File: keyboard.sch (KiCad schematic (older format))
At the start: 149 parts

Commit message: Minor Changes On Schematic
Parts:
- gave numbers to parts that had none: 2
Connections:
- wire segments 325 -> 261
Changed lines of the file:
@@
 $EndComp
 $Comp
-L D D?
+L D D05
 U 1 1 57519F72
 P 3150 8400
-F 0 "D?" H 3150 8500 50  0000 C CNN
+F 0 "D05" H 3150 8500 50  0000 C CNN
 F 1 "D" H 3150 8300 50  0000 C CNN
 F 2 "" H 3150 8400 50  0000 C CNN
@@
 $EndComp
 $Comp
-L D D?
+L D D10
 U 1 1 57519F81
 P 3900 8600
-F 0 "D?" H 3900 8700 50  0000 C CNN
+F 0 "D10" H 3900 8700 50  0000 C CNN
 F 1 "D" H 3900 8500 50  0000 C CNN
 F 2 "" H 3900 8600 50  0000 C CNN
@@
 	11850 2650 12050 2650
 Wire Wire Line
-	13200 2400 13200 2600
-Wire Wire Line
-	13200 2600 13200 2800
+	13200 2400 13200 2800
 Wire Wire Line
 	12600 2800 12800 2800
@@
 	11850 4050 12050 4050
 Wire Wire Line
-	3450 5150 3450 5350
-Wire Wire Line
-	3450 5350 3450 5600
+	3450 5150 3450 5600
 Wire Wire Line
 	4200 5150 4200 5400
@@
 	11100 5400 11300 5400
 Wire Wire Line
-	12450 5150 12450 5350
-Wire Wire Line
-	12450 5350 12450 5400
-Wire Wire Line
-	3450 6500 3450 6750
-Wire Wire Line
-	3450 6750 3450 7000
+	12450 5150 12450 5400
+Wire Wire Line
+	3450 6500 3450 7000
 Wire Wire Line
 	4200 6500 4200 6750
@@
 	11100 6750 11300 6750
 Wire Wire Line
-	12450 6500 12450 6700
-Wire Wire Line
-	12450 6700 12450 7000
+	12450 6500 12450 7000
 Wire Wire Line
 	12450 7000 12350 7000
@@
 	11850 7000 12050 7000
 Wire Wire Line
-	3450 7900 3450 8150
-Wire Wire Line
-	3450 8150 3450 8400
-Wire Wire Line
-	4200 7900 4200 8150
-Wire Wire Line
-	4200 8150 4200 8200
-Wire Wire Line
-	4950 7900 4950 8150
-Wire Wire Line
-	4950 8150 4950 8400
-Wire Wire Line
-	7200 7900 7200 8150
-Wire Wire Line
-	7200 8150 7200 8350
-Wire Wire Line
-	7200 8350 7200 8550
+	3450 7900 3450 8400
+Wire Wire Line
+	4200 7900 4200 8200
+Wire Wire Line
+	4950 7900 4950 8400
+Wire Wire Line
+	7200 7900 7200 8550
 Wire Wire Line
 	10200 7900 10200 8150
@@
 	9600 8150 9800 8150
 Wire Wire Line
-	10950 7900 10950 8150
-Wire Wire Line
-	10950 8150 10950 8400
-Wire Wire Line
-	11700 7900 11700 8150
-Wire Wire Line
-	11700 8150 11700 8400
-Wire Wire Line
-	11700 8400 11700 8650
-Wire Wire Line
-	12450 7900 12450 8150
-Wire Wire Line
-	12450 8150 12450 8500
-Wire Wire Line
-	13200 7900 13200 8100
-Wire Wire Line
-	13200 8100 13200 8450
-Wire Wire Line
-	1650 2150 3050 2150
-Wire Wire Line
-	3050 2150 3800 2150
-Wire Wire Line
-	3800 2150 12700 2150
-Wire Wire Line
-	12700 2150 13850 2150
-Wire Wire Line
-	1650 3550 3050 3550
-Wire Wire Line
-	3050 3550 13850 3550
-Wire Wire Line
-	1650 4900 2950 4900
-Wire Wire Line
-	2950 4900 3050 4900
-Wire Wire Line
-	3050 4900 11950 4900
-Wire Wire Line
-	11950 4900 12650 4900
-Wire Wire Line
-	12650 4900 12700 4900
-Wire Wire Line
-	12700 4900 13200 4900
-Wire Wire Line
-	13200 4900 13850 4900
-Wire Wire Line
-	1650 6250 2950 6250
-Wire Wire Line
-	2950 6250 3050 6250
-Wire Wire Line
-	3050 6250 11950 6250
-Wire Wire Line
-	11950 6250 13850 6250
-Wire Wire Line
-	1650 7650 2900 7650
-Wire Wire Line
-	2900 7650 2950 7650
-Wire Wire Line
-	2950 7650 3050 7650
-Wire Wire Line
-	3050 7650 3650 7650
-Wire Wire Line
-	3650 7650 3700 7650
-Wire Wire Line
-	3700 7650 3800 7650
-Wire Wire Line
-	3800 7650 4450 7650
-Wire Wire Line
-	4450 7650 6650 7650
-Wire Wire Line
-	6650 7650 6700 7650
-Wire Wire Line
-	6700 7650 10450 7650
-Wire Wire Line
-	10450 7650 11150 7650
-Wire Wire Line
-	11150 7650 11200 7650
-Wire Wire Line
-	11200 7650 11950 7650
-Wire Wire Line
-	11950 7650 12700 7650
-Wire Wire Line
-	12700 7650 13850 7650
-Wire Wire Line
-	2850 1500 2850 2650
-Wire Wire Line
-	2850 2650 2850 4050
-Wire Wire Line
-	2850 4050 2850 5600
-Wire Wire Line
-	2850 5600 2850 7000
-Wire Wire Line
-	2850 7000 2850 8400
-Wire Wire Line
-	2850 8400 2850 9200
-Wire Wire Line
-	3600 1500 3600 2650
-Wire Wire Line
-	3600 2650 3600 8600
-Wire Wire Line
-	3600 8600 3600 9200
-Wire Wire Line
-	4350 1500 4350 8400
-Wire Wire Line
-	4350 8400 4350 9200
+	10950 7900 10950 8400
+Wire Wire Line
+	11700 7900 11700 8650
+Wire Wire Line
+	12450 7900 12450 8500
+Wire Wire Line
+	13200 7900 13200 8450
+Wire Wire Line
+	1650 2150 13850 2150
+Wire Wire Line
+	1650 3550 13850 3550
+Wire Wire Line
+	1650 4900 13850 4900
+Wire Wire Line
+	1650 6250 13850 6250
+Wire Wire Line
+	1650 7650 13850 7650
+Wire Wire Line
+	2850 1500 2850 9200
+Wire Wire Line
+	3600 1500 3600 9200
+Wire Wire Line
+	4350 1500 4350 9200
 Wire Wire Line
 	5100 1500 5100 9200
@@
 	5850 1500 5850 9200
 Wire Wire Line
-	6600 1500 6600 8550
-Wire Wire Line
-	6600 8550 6600 9200
+	6600 1500 6600 9200
 Wire Wire Line
 	7350 1500 7350 9200
@@
 	9600 1500 9600 9200
 Wire Wire Line
-	10350 1500 10350 8400
-Wire Wire Line
-	10350 8400 10350 9200
-Wire Wire Line
-	11100 1500 11100 8650
-Wire Wire Line
-	11100 8650 11100 9200
-Wire Wire Line
-	11850 1500 11850 5400
-Wire Wire Line
-	11850 5400 11850 8500
-Wire Wire Line
-	11850 8500 11850 9200
-Wire Wire Line
-	12600 1500 12600 4050
-Wire Wire Line
-	12600 4050 12600 5800
-Wire Wire Line
-	12600 5800 12600 8450
-Wire Wire Line
-	12600 8450 12600 9200
+	10350 1500 10350 9200
+Wire Wire Line
+	11100 1500 11100 9200
+Wire Wire Line
+	11850 1500 11850 9200
+Wire Wire Line
+	12600 1500 12600 9200
 Wire Wire Line
 	13200 2800 13100 2800
@@
 Connection ~ 12650 4900
 Wire Wire Line
-	13200 4900 13200 5150
-Wire Wire Line
-	13200 5150 13200 5350
-Wire Wire Line
-	13200 5350 13200 5550
-Wire Wire Line
-	13200 5550 13200 5800
+	13200 4900 13200 5800
 Connection ~ 13200 4900
 Wire Wire Line
@@
 Connection ~ 12600 5800
 Wire Wire Line
-	13200 6500 13200 6700
-Wire Wire Line
-	13200 6700 13200 6900
-Wire Wire Line
-	13200 6900 13200 7150
+	13200 6500 13200 7150
 Wire Wire Line
 	12700 6250 12700 6450
@@
 Connection ~ 3700 7650
 Wire Wire Line
-	4200 8150 4200 8350
-Wire Wire Line
-	4200 8350 4200 8600
+	4200 8150 4200 8600
 Wire Wire Line
 	4200 8350 4050 8350
@@
 Connection ~ 6800 7650
 Connection ~ 4550 7650
+Connection ~ 12800 4900
 $EndSCHEMATC

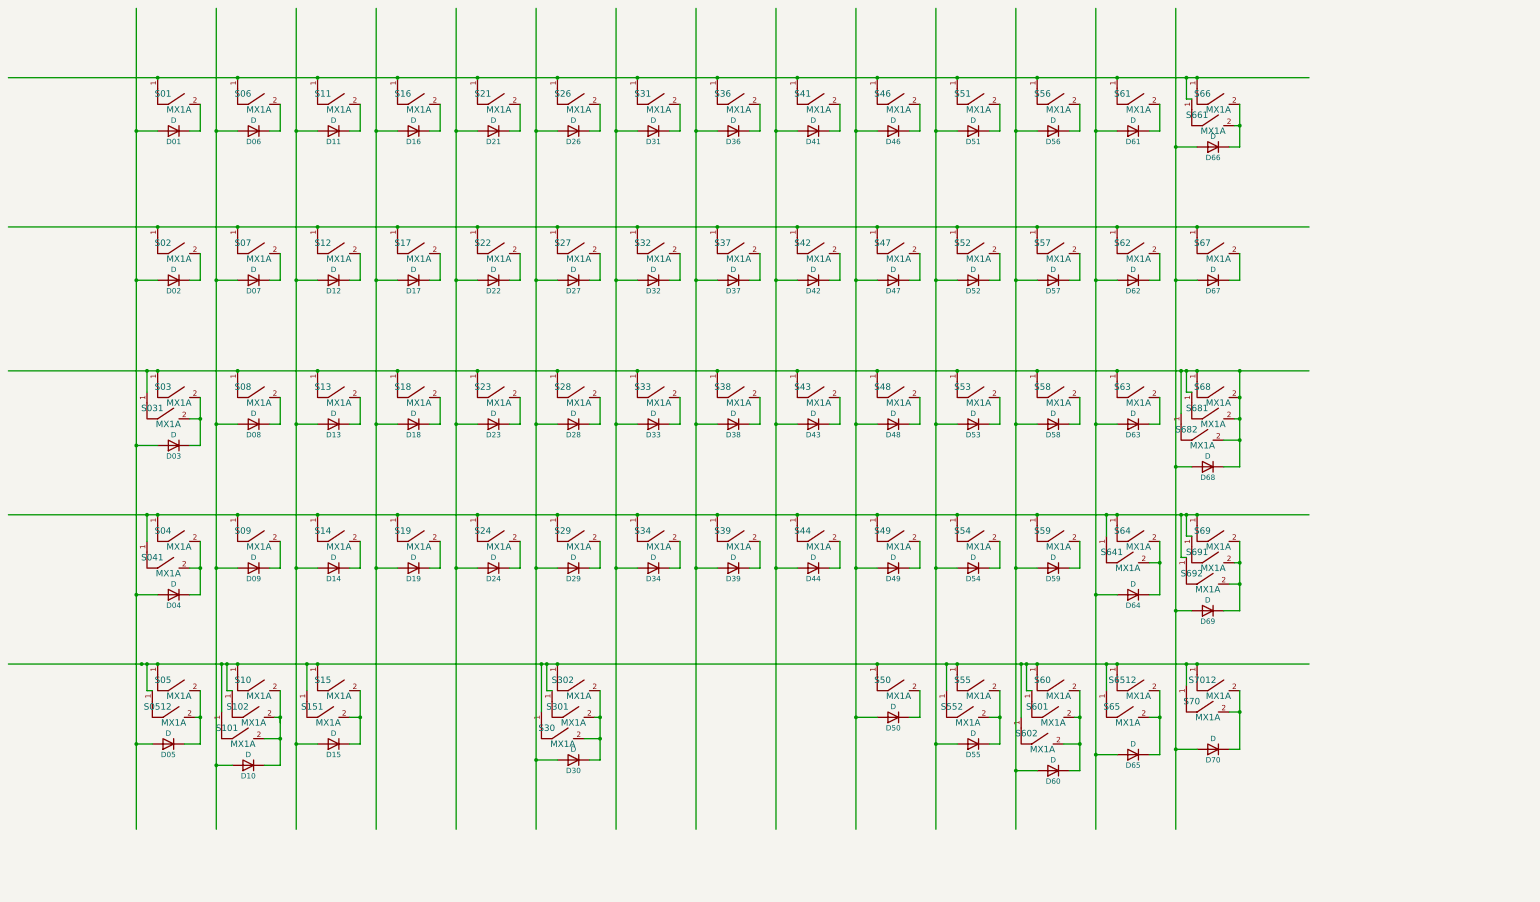
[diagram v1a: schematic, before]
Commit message: Complete LED Matrix
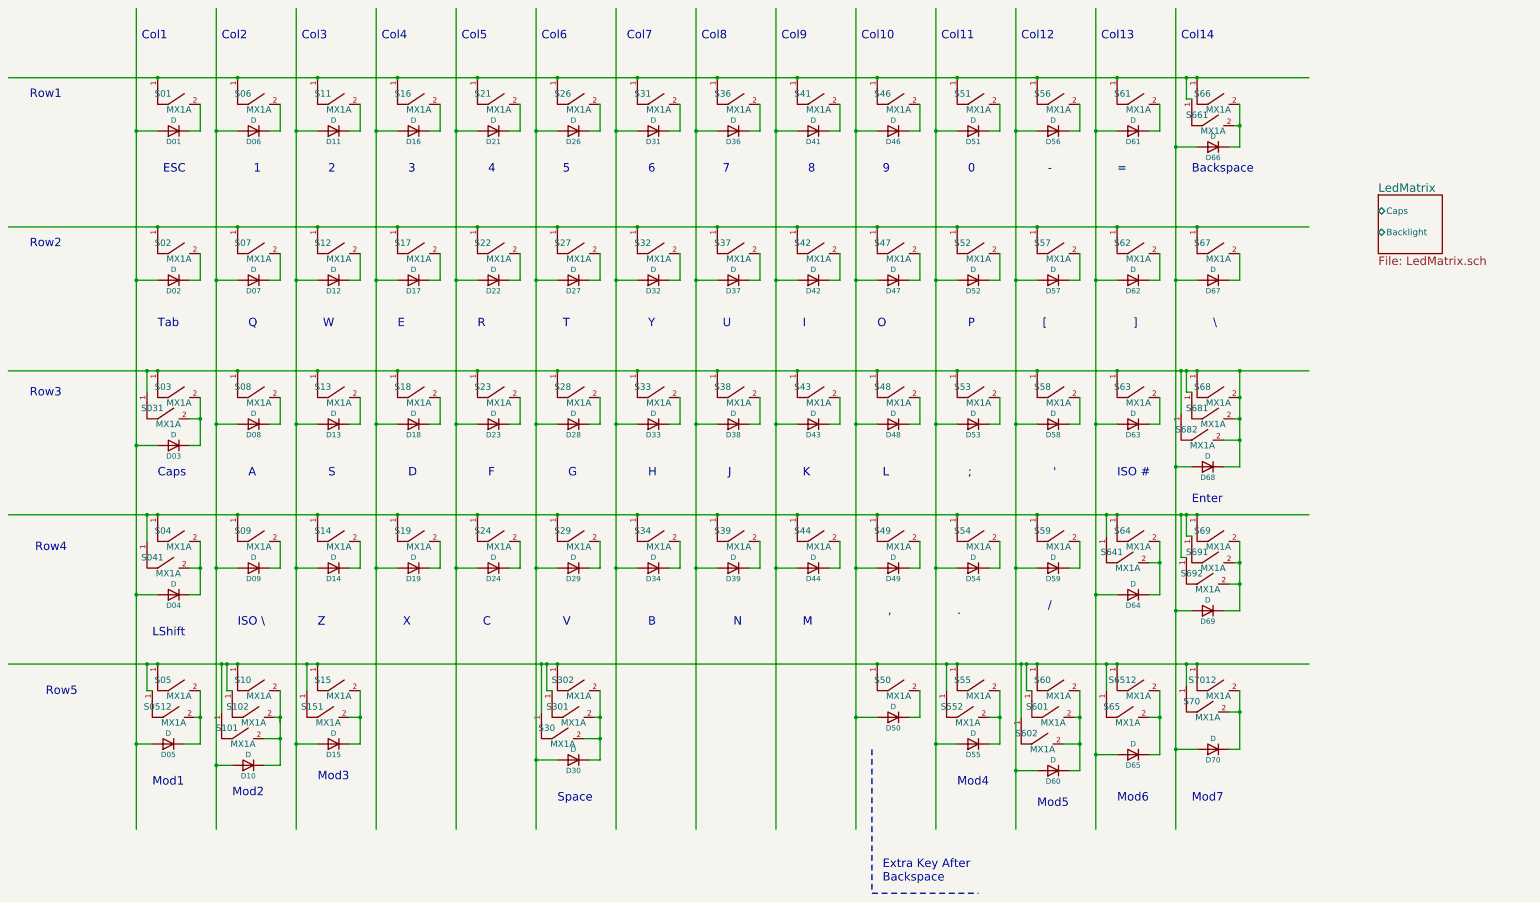
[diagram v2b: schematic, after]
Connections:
- wire segments 261 -> 431
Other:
- note added: "'"
- note added: ","
- note added: "-"
- note added: "."
- note added: "/"
- note added: "0"
- note added: "1\n"
- note added: "2\n"
- note added: "3"
- note added: "4"
- note added: "5"
- note added: "6"
- note added: "7"
- note added: "8\n"
- note added: "9"
- note added: ";"
- note added: "="
- note added: "A"
- note added: "B"
- note added: "Backspace"
- note added: "C"
- note added: "Caps"
- note added: "Col1"
- note added: "Col10"
- note added: "Col11"
- note added: "Col12"
- note added: "Col13"
- note added: "Col14"
- note added: "Col2\n"
- note added: "Col3\n"
- note added: "Col4"
- note added: "Col5"
- note added: "Col6"
- note added: "Col7"
- note added: "Col8"
- note added: "Col9"
- note added: "D"
- note added: "E"
- note added: "ESC"
- note added: "Enter"
- note added: "Extra Key After \nBackspace"
- note added: "F"
- note added: "G"
- note added: "H"
- note added: "I"
- note added: "ISO #"
- note added: "ISO \\n"
- note added: "J"
- note added: "K"
- note added: "L"
- note added: "LShift\n"
- note added: "M"
- note added: "Mod1\n"
- note added: "Mod2\n"
- note added: "Mod3"
- note added: "Mod4"
- note added: "Mod5"
- note added: "Mod6"
- note added: "Mod7"
- note added: "N"
- note added: "O"
- note added: "P"
- note added: "Q"
- note added: "R"
- note added: "Row1"
- note added: "Row2"
- note added: "Row3"
- note added: "Row4"
- note added: "Row5"
- note added: "S"
- note added: "Space"
- note added: "T"
- note added: "Tab"
- note added: "U"
- note added: "V"
- note added: "W"
- note added: "X"
- note added: "Y"
- note added: "Z"
- note added: "["
- note added: "\"
- note added: "]"

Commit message: Add PCB file
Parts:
- added HOLE1, HOLE2, HOLE3: HOLE, holes:PKRH, symbol ANYTHING
- added HOLE4: HOLE, holes:PKRHC, symbol ANYTHING
- added HOLE5, HOLE6: HOLE, holes:PKRHSL, symbol ANYTHING
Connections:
- wire segments 431 -> 261
